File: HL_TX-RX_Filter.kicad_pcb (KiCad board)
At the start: 2 copper layers, 100 x 100 mm, 199 parts, among them J1 CNR1, J10 To Rx in, J2 CNR3, J3 CNR2, J4 CNR4, J5 To Antenna, J6 From Tx, J7 ICSP, J8 SCL SDA, J9 Input1, Q1 2N7002, Q2 2N7002, Q3 2N7002, Q4 2N7002, Q5 2N7002, Q6 2N7002, Q7 2N7002, Q8 2N7002, U1 ATMEGA328-AU, U10 PE4259, U11 PE4259, U12 PE4259, U2 PE4259, U3 PE4259, U4 PE4259, U5 PE4259, U6 PE4259, U7 PE4259, U8 PE4259, U9 PE4259

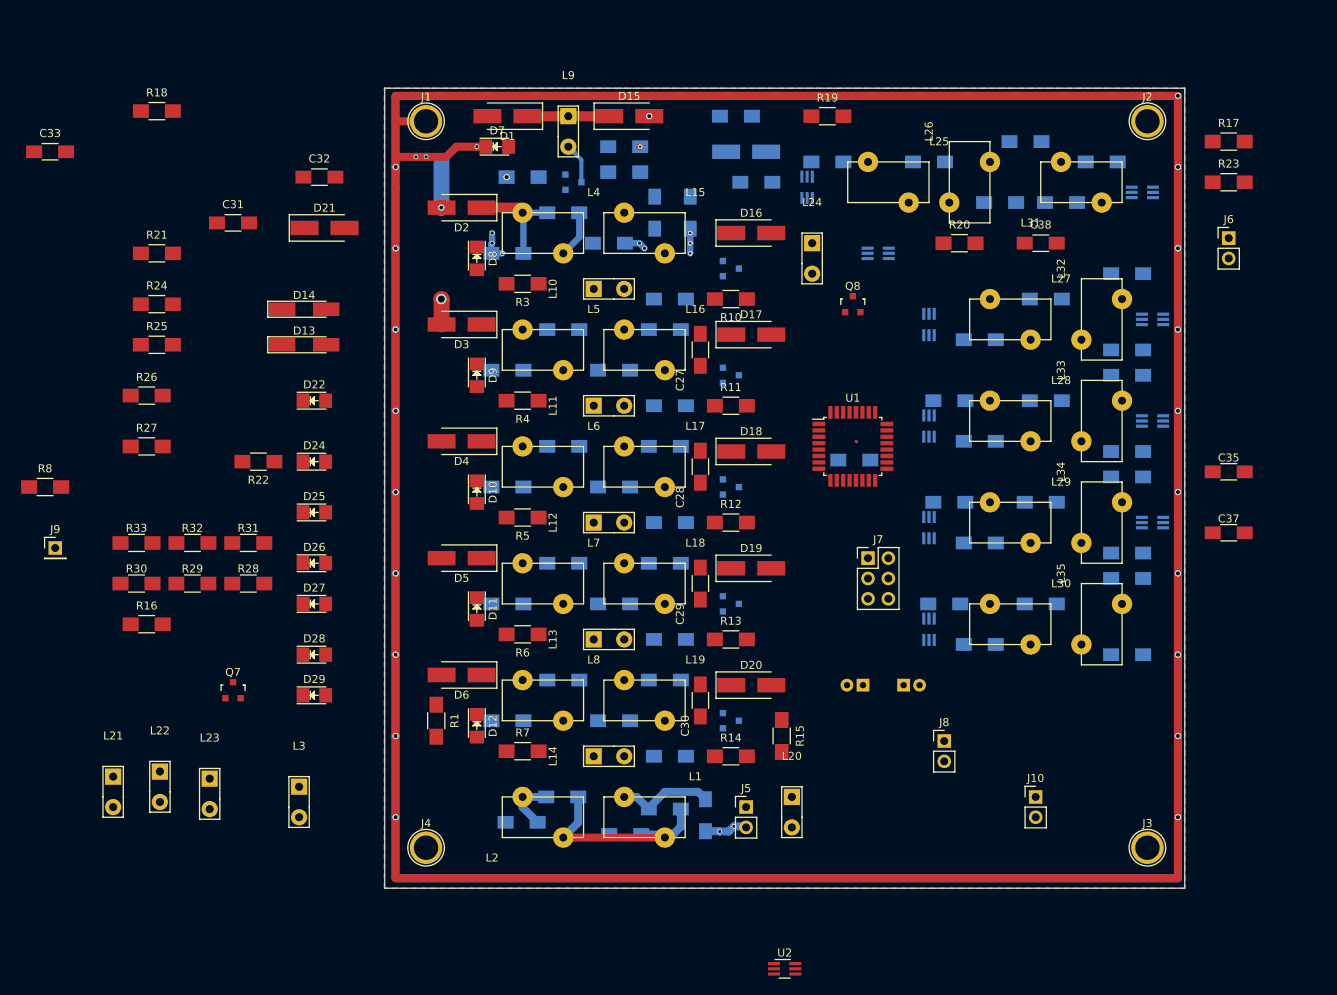
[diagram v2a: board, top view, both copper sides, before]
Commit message: Re-building PCB after annotation redo
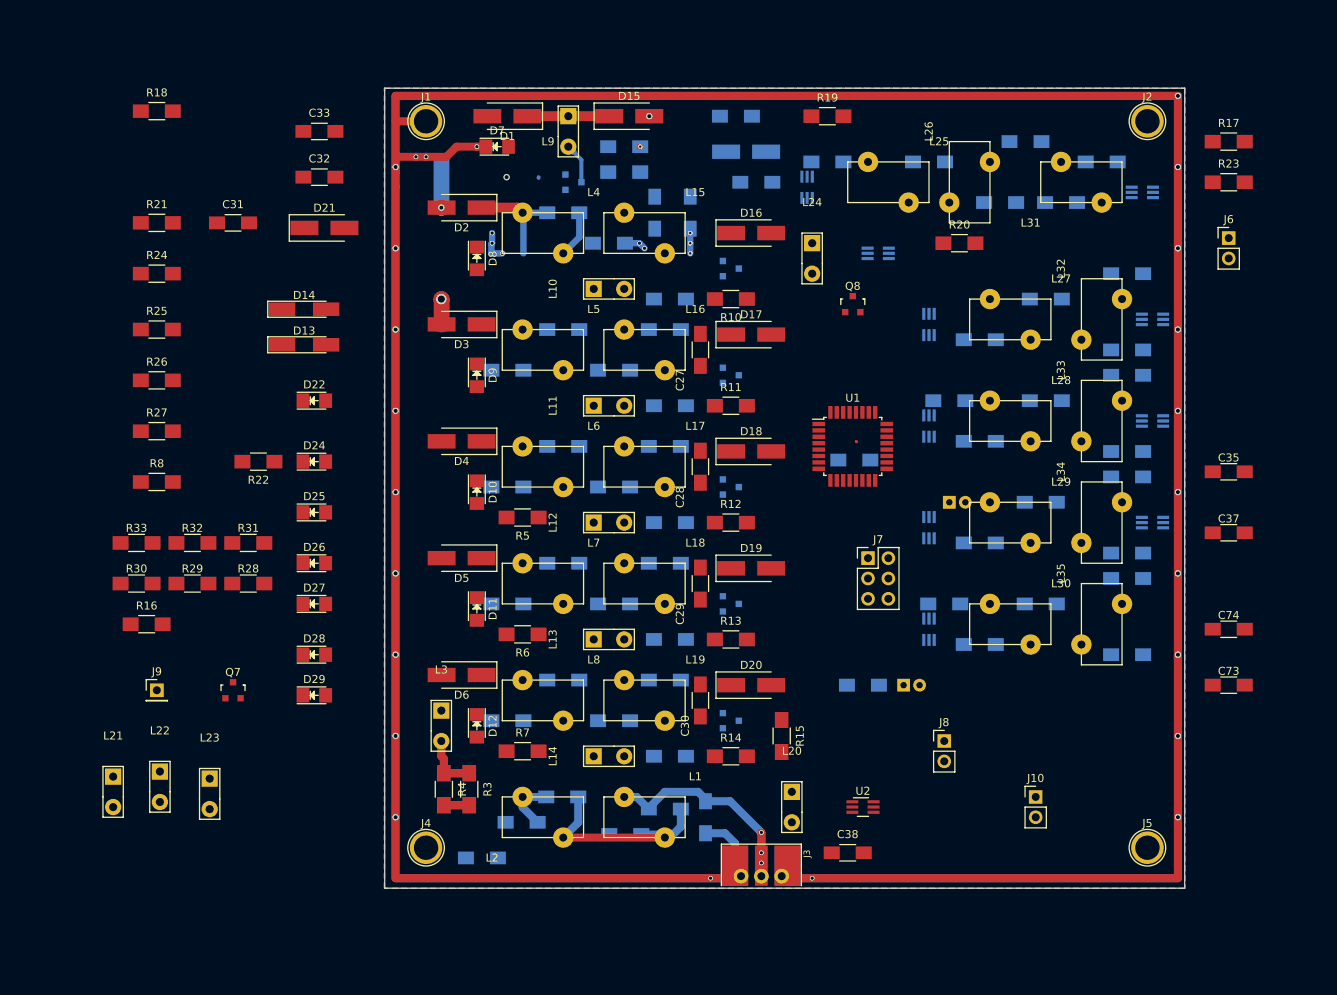
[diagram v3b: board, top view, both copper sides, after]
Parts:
- added C73: 680p, Capacitors_SMD:C_1206_HandSoldering, F.Cu at (230.5, 134.6)
- added C74: 360p, Capacitors_SMD:C_1206_HandSoldering, F.Cu at (230.5, 127.6)
- C10: value 1000p -> 540p
- C11: value 15p -> 1000p
- C12: value 39p -> 15p
- C13: value 68p -> 39p
- C14: value 82p -> 68p
- C15: value 180p -> 82p
- C16: value .1u -> 180p
- C22: value 300p -> .1u
- C23: value 560p -> 300p
- C24: value 1082p -> 560p
- C25: value 2100p -> 1082p
- C26: value 200p -> 2100p
- C27: value 43p -> 200p
- C28: value 130p -> 43p
- C29: value 220p -> 130p
- C30: value 270p -> 220p
- C31: value 552p -> 270p
- C32: value 74p -> 552p
- C33: value 120p -> 74p
- C34: value 180p -> 120p
- C35: value 390p -> 180p
- C36: value 736p -> 390p
- C37: value 22p -> 736p
- C38: value C -> .1u
- C39: value 0.1u -> 22p
- C40: value 0.1 -> C
- C41: value 4.7u -> 0.1u; footprint Capacitors_THT:CP_Radial_D5.0mm_P2.00mm -> Capacitors_SMD:C_1206_HandSoldering
- C42: value C -> 0.1
- C44: value 0.1u -> C
- C45: value 0.1u -> 4.7u; footprint Capacitors_SMD:C_1206_HandSoldering -> Capacitors_THT:CP_Radial_D5.0mm_P2.00mm
- C46: value 3000p -> 0.1u
- C47: value 0.012u -> 0.1u
- C48: value 1600p -> 3000p
- C49: value 1500p -> 0.012u
- C50: value 680p -> 1600p
- C51: value 470p -> 1500p
- C52: value 270p -> 680p
- C53: value 2400p -> 470p
- C54: value 8200p -> 270p
- C55: value 3900p -> 2400p
- C56: value 2400p -> 8200p
- C57: value 1500p -> 3900p
- C58: value 1800p -> 2400p
- C59: value 680p -> 1500p
- C6: value 100p -> .1u
- C60: value 340p -> 1800p
- C61: value 236p -> 680p
- C62: value 130p -> 340p
- C63: value 3000p -> 236p
- C64: value 2700p -> 130p
- C65: value 1220p -> 3000p
- C66: value 780p -> 2700p
- C67: value 510p -> 1220p
- C68: value 2400p -> 780p
- C69: value 2000p -> 510p
- C7: value 150p -> 100p
- C70: value 1000p -> 2400p
- C71: value 680p -> 2000p
- C72: value 360p -> 1000p
- C8: value 280p -> 150p
- C9: value 540p -> 280p
- J3: value CNR2 -> Antenna; footprint Connectors:1pin -> Connectors_G:SMAEDGE_TH
- J4: value CNR4 -> CNR2
- J5: value To Antenna -> CNR4; footprint Pin_Headers:Pin_Header_Straight_1x02_Pitch2.54mm -> Connectors:1pin
- R1: moved to B.Cu
- moved C38 79.9 mm to (182.9, 155.6)
- moved R2 77.1 mm to (132.4, 147.6), turned to 270 degrees
- moved C6 75.6 mm to (137.2, 156.2)
- moved R3 63.5 mm to (135.6, 147.6), turned to 270 degrees
- moved J5 50.4 mm to (220.3, 154.9)
- moved R4 49.6 mm to (132.4, 147.6), turned to 270 degrees
- moved J3 48.5 mm to (172.1, 159.9)
- moved C33 33.8 mm to (116.8, 65.4)
- moved U2 22.5 mm to (184.8, 149.9)
- moved J9 21.8 mm to (96.5, 135.3)
- moved L3 20.2 mm to (132.1, 137.8)
- moved R8 14.0 mm to (96.5, 109.2)
- moved R1 9.51 mm to (135.6, 147.6)
- moved R21 3.81 mm to (96.5, 76.8)
- moved R24 3.81 mm to (96.5, 83.2)
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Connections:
- C11 pad 2: Net-(C11-Pad2) -> GND
- C16 pad 1: Net-(C16-Pad1) -> Net-(C11-Pad1)
- C16 pad 2: GND -> Net-(C16-Pad2)
- C22 pad 1: Net-(C12-Pad2) -> Net-(C22-Pad1)
- C26 pad 1: Net-(C11-Pad2) -> Net-(C16-Pad2)
- C27 pad 1: Net-(C11-Pad2) -> Net-(C12-Pad2)
- C27 pad 2: Net-(C27-Pad2) -> GND
- C32 pad 1: Net-(C27-Pad2) -> Net-(C16-Pad2)
- C32 pad 2: GND -> Net-(C32-Pad2)
- C37 pad 1: Net-(C37-Pad1) -> Net-(C32-Pad2)
- C37 pad 2: Net-(C37-Pad2) -> GND
- C38 pad 1: Net-(C38-Pad1) -> GND
- C39 pad 1: Net-(C37-Pad2) -> Net-(C39-Pad1)
- C40 pad 1: 3V3 -> Net-(C40-Pad1)
- C40 pad 2: GND -> Net-(C40-Pad2)
- C41 pad 1: 3V3 -> Net-(C39-Pad2)
- C41 pad 2: GND -> Net-(C41-Pad2)
- C42 pad 1: Net-(C38-Pad1) -> 3V3
- C42 pad 2: Net-(C42-Pad2) -> GND
- C44 pad 1: Net-(C44-Pad1) -> Net-(C40-Pad1)
- C44 pad 2: GND -> Net-(C44-Pad2)
- C45 pad 1: Net-(C45-Pad1) -> 3V3
- C45 pad 2: Net-(C45-Pad2) -> GND
- C46 pad 2: Net-(C46-Pad2) -> GND
- C47 pad 2: GND -> Net-(C47-Pad2)
- C48 pad 1: Net-(C46-Pad2) -> Net-(C48-Pad1)
- C49 pad 2: Net-(C49-Pad2) -> GND
- C50 pad 1: Net-(C50-Pad1) -> Net-(C48-Pad2)
- C53 pad 2: GND -> Net-(C53-Pad2)
- C54 pad 2: GND -> Net-(C54-Pad2)
- C58 pad 1: Net-(C48-Pad2) -> Net-(C58-Pad1)
- C58 pad 2: Net-(C58-Pad2) -> GND
- C59 pad 1: Net-(C49-Pad2) -> Net-(C59-Pad1)
- C59 pad 2: Net-(C59-Pad2) -> GND
- C6 pad 1: Net-(C11-Pad1) -> GND
- C6 pad 2: GND -> Net-(C38-Pad2)
- C63 pad 1: Net-(C63-Pad1) -> Net-(C53-Pad2)
- C63 pad 2: GND -> Net-(C63-Pad2)
- C64 pad 1: Net-(C64-Pad1) -> Net-(C54-Pad2)
- C64 pad 2: GND -> Net-(C64-Pad2)
- C68 pad 1: Net-(C58-Pad2) -> Net-(C68-Pad1)
- C68 pad 2: Net-(C68-Pad2) -> GND
- C69 pad 1: Net-(C59-Pad2) -> Net-(C69-Pad1)
- C69 pad 2: Net-(C69-Pad2) -> GND
- D13 pad 1: Net-(C37-Pad1) -> Net-(C39-Pad1)
- D14 pad 1: Net-(C44-Pad1) -> Net-(C46-Pad1)
- D14 pad 2: Net-(C37-Pad1) -> Net-(C39-Pad1)
- D15 pad 2: Net-(C38-Pad1) -> Net-(C40-Pad1)
- D16 pad 1: Net-(C27-Pad2) -> Net-(C28-Pad2)
- D16 pad 2: Net-(C38-Pad1) -> Net-(C40-Pad1)
- D17 pad 1: Net-(C28-Pad2) -> Net-(C29-Pad2)
- D17 pad 2: Net-(C38-Pad1) -> Net-(C40-Pad1)
- D18 pad 1: Net-(C29-Pad2) -> Net-(C30-Pad2)
- D18 pad 2: Net-(C38-Pad1) -> Net-(C40-Pad1)
- D19 pad 1: Net-(C30-Pad2) -> Net-(C31-Pad2)
- D19 pad 2: Net-(C38-Pad1) -> Net-(C40-Pad1)
- D2 pad 1: Net-(C11-Pad1) -> Net-(C12-Pad1)
- D20 pad 1: Net-(C31-Pad2) -> Net-(C32-Pad2)
- D20 pad 2: Net-(C38-Pad1) -> Net-(C40-Pad1)
- D21 pad 1: Net-(C37-Pad2) -> Net-(C39-Pad2)
- D21 pad 2: Net-(C38-Pad2) -> Net-(C40-Pad2)
- D23 pad 1: Net-(C45-Pad1) -> Net-(C47-Pad1)
- D23 pad 2: Net-(C42-Pad2) -> Net-(C44-Pad2)
- D3 pad 1: Net-(C12-Pad1) -> Net-(C13-Pad1)
- D4 pad 1: Net-(C13-Pad1) -> Net-(C14-Pad1)
- D5 pad 1: Net-(C14-Pad1) -> Net-(C10-Pad1)
- D6 pad 1: Net-(C10-Pad1) -> Net-(C11-Pad1)
- J3 pad 1: GND -> Net-(C1-Pad2)
- J5 pad 1: Net-(C1-Pad2) -> GND
- J6 pad 1: Net-(C39-Pad2) -> Net-(C41-Pad2)
- L10 pad 1: Net-(C11-Pad2) -> Net-(C12-Pad2)
- L10 pad 2: Net-(C17-Pad1) -> Net-(C18-Pad1)
- L11 pad 1: Net-(C12-Pad2) -> Net-(C13-Pad2)
- L11 pad 2: Net-(C18-Pad1) -> Net-(C19-Pad1)
- L12 pad 1: Net-(C13-Pad2) -> Net-(C14-Pad2)
- L12 pad 2: Net-(C19-Pad1) -> Net-(C20-Pad1)
- L13 pad 1: Net-(C14-Pad2) -> Net-(C15-Pad2)
- L13 pad 2: Net-(C20-Pad1) -> Net-(C21-Pad1)
- L14 pad 1: Net-(C15-Pad2) -> Net-(C16-Pad2)
- L14 pad 2: Net-(C21-Pad1) -> Net-(C22-Pad1)
- L15 pad 1: Net-(C11-Pad2) -> Net-(C12-Pad2)
- L15 pad 2: Net-(C27-Pad2) -> Net-(C28-Pad2)
- L16 pad 1: Net-(C12-Pad2) -> Net-(C13-Pad2)
- L16 pad 2: Net-(C28-Pad2) -> Net-(C29-Pad2)
- L17 pad 1: Net-(C13-Pad2) -> Net-(C14-Pad2)
- L17 pad 2: Net-(C29-Pad2) -> Net-(C30-Pad2)
- L18 pad 1: Net-(C14-Pad2) -> Net-(C15-Pad2)
- L18 pad 2: Net-(C30-Pad2) -> Net-(C31-Pad2)
- L19 pad 1: Net-(C15-Pad2) -> Net-(C16-Pad2)
- L19 pad 2: Net-(C31-Pad2) -> Net-(C32-Pad2)
- L20 pad 1: Net-(L20-Pad1) -> Net-(C40-Pad1)
- L22 pad 1: Net-(C37-Pad2) -> Net-(C39-Pad2)
- L24 pad 1: Net-(C45-Pad1) -> Net-(C47-Pad1)
- L25 pad 1: Net-(C47-Pad1) -> Net-(C49-Pad1)
- L25 pad 2: Net-(C46-Pad2) -> Net-(C48-Pad2)
- L26 pad 1: Net-(C48-Pad2) -> Net-(C50-Pad2)
- L26 pad 2: Net-(C53-Pad1) -> Net-(C55-Pad1)
- L27 pad 1: Net-(C54-Pad1) -> Net-(C56-Pad1)
- L27 pad 2: Net-(C49-Pad2) -> Net-(C51-Pad2)
- L28 pad 1: Net-(C55-Pad1) -> Net-(C57-Pad1)
- L28 pad 2: Net-(C50-Pad2) -> Net-(C52-Pad2)
- L29 pad 1: Net-(C56-Pad1) -> Net-(C58-Pad1)
- L29 pad 2: Net-(C51-Pad2) -> Net-(C53-Pad2)
- L3 pad 1: Net-(L3-Pad1) -> Net-(C2-Pad1)
- L3 pad 2: Net-(L20-Pad2) -> Net-(L3-Pad2)
- L30 pad 1: Net-(C57-Pad1) -> Net-(C59-Pad1)
- L30 pad 2: Net-(C52-Pad2) -> Net-(C54-Pad2)
- L31 pad 1: Net-(C58-Pad2) -> Net-(C60-Pad2)
- L31 pad 2: Net-(C63-Pad1) -> Net-(C65-Pad1)
- L32 pad 1: Net-(C59-Pad2) -> Net-(C61-Pad2)
- L32 pad 2: Net-(C64-Pad1) -> Net-(C66-Pad1)
- L33 pad 1: Net-(C60-Pad2) -> Net-(C62-Pad2)
- L33 pad 2: Net-(C65-Pad1) -> Net-(C67-Pad1)
- L34 pad 1: Net-(C61-Pad2) -> Net-(C63-Pad2)
- L34 pad 2: Net-(C66-Pad1) -> Net-(C68-Pad1)
- L35 pad 1: Net-(C62-Pad2) -> Net-(C64-Pad2)
- L35 pad 2: Net-(C67-Pad1) -> Net-(C69-Pad1)
- L4 pad 1: Net-(C11-Pad2) -> Net-(C12-Pad2)
- L4 pad 2: Net-(C11-Pad1) -> Net-(C12-Pad1)
- L5 pad 1: Net-(C12-Pad2) -> Net-(C13-Pad2)
- L5 pad 2: Net-(C12-Pad1) -> Net-(C13-Pad1)
- L6 pad 1: Net-(C13-Pad2) -> Net-(C14-Pad2)
- L6 pad 2: Net-(C13-Pad1) -> Net-(C14-Pad1)
- L7 pad 1: Net-(C14-Pad2) -> Net-(C15-Pad2)
- L7 pad 2: Net-(C14-Pad1) -> Net-(C10-Pad1)
- L8 pad 1: Net-(C15-Pad2) -> Net-(C16-Pad2)
- L8 pad 2: Net-(C10-Pad1) -> Net-(C11-Pad1)
- L9 pad 2: Net-(C16-Pad1) -> Net-(C17-Pad1)
- Q1 pad 3: Net-(C16-Pad1) -> Net-(C17-Pad1)
- Q2 pad 3: Net-(C17-Pad1) -> Net-(C18-Pad1)
- Q3 pad 3: Net-(C18-Pad1) -> Net-(C19-Pad1)
- Q4 pad 3: Net-(C19-Pad1) -> Net-(C20-Pad1)
- Q5 pad 3: Net-(C20-Pad1) -> Net-(C21-Pad1)
- Q6 pad 3: Net-(C21-Pad1) -> Net-(C22-Pad1)
- R1 pad 1: Net-(C2-Pad1) -> Net-(L3-Pad2)
- R1 pad 2: Net-(L3-Pad1) -> Net-(C38-Pad2)
- R11 pad 2: (no net) -> +12V
- R12 pad 1: Net-(C44-Pad1) -> Net-(C46-Pad1)
- R12 pad 2: Net-(C16-Pad1) -> Net-(C17-Pad1)
- R13 pad 1: Net-(C44-Pad1) -> Net-(C46-Pad1)
- R13 pad 2: Net-(C17-Pad1) -> Net-(C18-Pad1)
- R14 pad 1: Net-(C44-Pad1) -> Net-(C46-Pad1)
- R14 pad 2: Net-(C18-Pad1) -> Net-(C19-Pad1)
- R15 pad 1: Net-(C44-Pad1) -> Net-(C46-Pad1)
- R15 pad 2: Net-(C19-Pad1) -> Net-(C20-Pad1)
- R16 pad 1: Net-(C44-Pad1) -> Net-(C46-Pad1)
- R16 pad 2: Net-(C20-Pad1) -> Net-(C21-Pad1)
- R17 pad 1: Net-(C44-Pad1) -> Net-(C46-Pad1)
- R17 pad 2: Net-(C21-Pad1) -> Net-(C22-Pad1)
- R18 pad 1: Net-(C38-Pad1) -> Net-(L20-Pad2)
- R18 pad 2: Net-(L20-Pad1) -> Net-(C38-Pad2)
- R19 pad 1: Net-(C38-Pad1) -> Net-(L20-Pad2)
- R19 pad 2: Net-(L20-Pad1) -> Net-(C38-Pad2)
- R2 pad 1: Net-(C2-Pad1) -> Net-(L3-Pad2)
- R2 pad 2: Net-(L3-Pad1) -> Net-(C38-Pad2)
- R20 pad 1: Net-(C38-Pad1) -> Net-(L20-Pad2)
- R20 pad 2: Net-(L20-Pad1) -> Net-(C38-Pad2)
- R21 pad 1: Net-(C38-Pad1) -> Net-(L20-Pad2)
- R21 pad 2: Net-(L20-Pad1) -> Net-(C38-Pad2)
- R22 pad 1: Net-(C38-Pad2) -> Net-(C40-Pad2)
- R23 pad 2: Net-(C44-Pad1) -> Net-(C46-Pad1)
- R25 pad 2: Net-(C42-Pad2) -> Net-(C44-Pad2)
- R26 pad 2: Net-(C44-Pad1) -> Net-(C46-Pad1)
- R3 pad 1: Net-(C2-Pad1) -> Net-(L3-Pad2)
- R3 pad 2: Net-(L3-Pad1) -> Net-(C38-Pad2)
- R4 pad 1: Net-(C2-Pad1) -> Net-(L3-Pad2)
- R4 pad 2: Net-(L3-Pad1) -> Net-(C38-Pad2)
- U1 pad 19: (no net) -> Net-(U1-Pad19)
- U1 pad 20: (no net) -> Net-(U1-Pad20)
- U1 pad 22: (no net) -> Net-(U1-Pad22)
- U1 pad 30: (no net) -> Net-(U1-Pad30)
- U1 pad 31: (no net) -> Net-(U1-Pad31)
- U10 pad 1: Net-(C70-Pad2) -> Net-(C72-Pad2)
- U10 pad 3: (no net) -> Net-(U10-Pad3)
- U11 pad 1: Net-(C71-Pad2) -> Net-(C73-Pad2)
- U11 pad 3: (no net) -> Net-(U11-Pad3)
- U12 pad 1: Net-(C72-Pad2) -> Net-(C74-Pad2)
- U12 pad 3: (no net) -> Net-(U12-Pad3)
- U2 pad 1: Net-(C46-Pad1) -> Net-(C48-Pad1)
- U2 pad 5: Net-(C45-Pad2) -> Net-(C47-Pad2)
- U3 pad 3: (no net) -> Net-(U3-Pad3)
- U4 pad 1: Net-(C49-Pad1) -> Net-(C51-Pad1)
- U4 pad 3: (no net) -> Net-(U4-Pad3)
- U5 pad 1: Net-(C50-Pad1) -> Net-(C52-Pad1)
- U5 pad 3: (no net) -> Net-(U5-Pad3)
- U6 pad 1: Net-(C51-Pad1) -> Net-(C53-Pad1)
- U6 pad 3: (no net) -> Net-(U6-Pad3)
- U7 pad 1: Net-(C52-Pad1) -> Net-(C54-Pad1)
- U7 pad 3: (no net) -> Net-(U7-Pad3)
- U8 pad 1: Net-(C68-Pad2) -> Net-(C70-Pad2)
- U8 pad 3: (no net) -> Net-(U8-Pad3)
- U9 pad 1: Net-(C69-Pad2) -> Net-(C71-Pad2)
- U9 pad 3: (no net) -> Net-(U9-Pad3)
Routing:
- net Net-(C1-Pad2): track 12.4 -> 32.1 mm, vias 0 -> 3
- net Net-(L3-Pad2): track 0.00 -> 14.7 mm
- net Net-(C12-Pad1): track 0.00 -> 13.6 mm
- net Net-(C11-Pad1): track 13.6 -> 0.13 mm
- net GND: track 813.9 -> 801.6 mm, vias 33 -> 28
- net Net-(C38-Pad2): track 0.00 -> 6.35 mm
- net Net-(C16-Pad1): track 6.15 -> 0.00 mm
- net Net-(C17-Pad1): track 0.00 -> 6.02 mm
- net Net-(C11-Pad2): track 5.91 -> 0.00 mm
- net (no net): track 0.06 -> 4.10 mm, vias 0 -> 4
- net Net-(C12-Pad2): track 0.00 -> 2.83 mm
- net Net-(C16-Pad2): track 0.00 -> 2.71 mm, vias 0 -> 2
- net Net-(C40-Pad1): track 0.00 -> 0.58 mm, vias 0 -> 1
- net 3V3: track 0.58 -> 0.00 mm
- net Net-(L3-Pad1): vias 1 -> 0
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
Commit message: Rearranging layout for re-annotated schematic
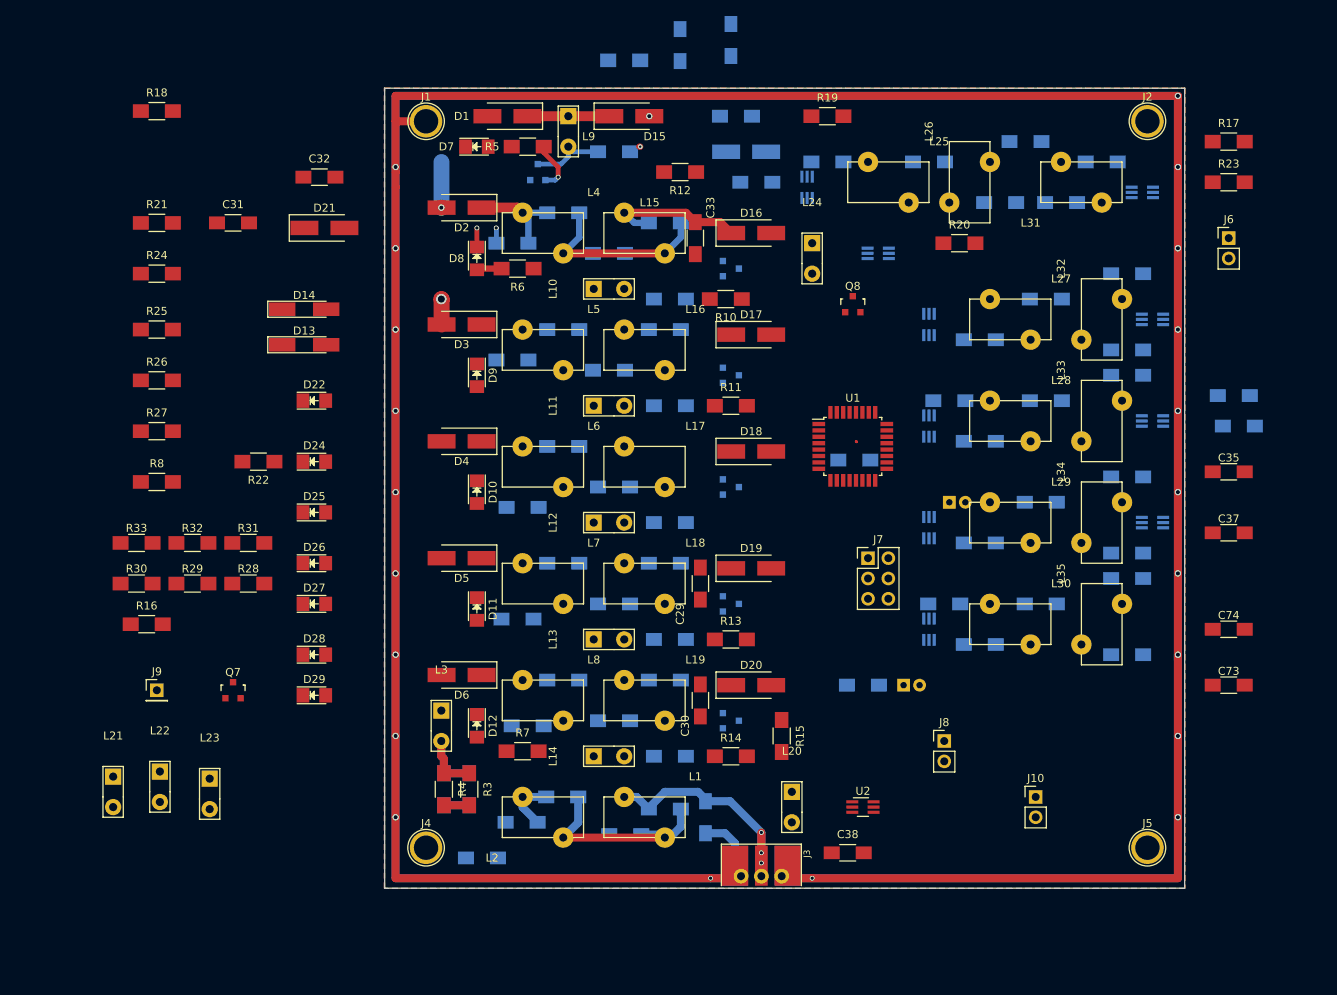
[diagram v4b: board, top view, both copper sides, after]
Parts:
- C27, C28: moved to B.Cu
- moved C67 84.4 mm to (231.8, 102.2)
- moved C11 64.3 mm to (142.9, 139.7)
- moved C16 54.9 mm to (147.3, 134.0)
- moved C33 48.8 mm to (163.8, 78.7), turned to 270 degrees
- moved R5 46.4 mm to (142.9, 67.3)
- moved R6 45.7 mm to (141.6, 82.5)
- moved R12 44.3 mm to (161.9, 70.5), turned to 180 degrees
- moved C28 30.8 mm to (160.0, 76.8), turned to 180 degrees
- moved C17 27.3 mm to (153.7, 67.9)
- moved C26 22.2 mm to (168.3, 54.0)
- moved C21 21.2 mm to (161.9, 54.6)
- moved C27 16.6 mm to (153.0, 80.6), turned to 0 degrees
- moved C7 15.9 mm to (141.0, 79.4)
- moved C8 15.9 mm to (141.0, 94.0)
- moved C59 15.1 mm to (231.1, 98.4)
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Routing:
- net Net-(C12-Pad2): track 2.83 -> 27.0 mm
- net Net-(C28-Pad2): track 0.00 -> 18.0 mm
- net GND: track 801.6 -> 787.3 mm, vias 28 -> 23
- net /T0: track 0.00 -> 6.30 mm, vias 0 -> 1
- net (no net): track 4.10 -> 0.15 mm, vias 4 -> 1
- net Net-(C17-Pad1): track 6.02 -> 9.43 mm
- net Net-(D8-Pad2): track 0.00 -> 3.14 mm
- net Net-(C16-Pad2): track 2.71 -> 0.00 mm, vias 2 -> 0
- net Net-(C12-Pad1): track 13.6 -> 12.7 mm

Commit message: More layout progress
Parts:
- C29, C30, C31, C32, R12, R13, R14, R15, R16, R17: moved to B.Cu
- C34, C36, R9: moved to F.Cu
- moved R17 99.9 mm to (168.3, 144.8), turned to 180 degrees
- moved C26 86.3 mm to (153.7, 139.1), turned to 0 degrees
- moved C71 80.8 mm to (230.5, 88.3)
- moved C32 77.3 mm to (160.0, 135.3), turned to 180 degrees
- moved C21 75.6 mm to (160.7, 130.2), turned to 0 degrees
- moved C68 75.6 mm to (229.2, 118.1)
- moved R16 73.1 mm to (168.3, 130.2), turned to 180 degrees
- moved R9 71.1 mm to (141.6, 126.4)
- moved C37 70.1 mm to (163.8, 137.2), turned to 270 degrees
- moved C31 69.5 mm to (160.0, 120.7), turned to 180 degrees
- moved C35 66.7 mm to (163.8, 108.0), turned to 270 degrees
- moved R10 60.5 mm to (141.6, 141.0)
- moved C36 59.3 mm to (163.8, 122.6), turned to 270 degrees
- moved R11 59.1 mm to (109.2, 99.1)
- moved C69 57.1 mm to (106.0, 83.2)
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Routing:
- net Net-(C46-Pad1): track 0.00 -> 93.7 mm
- net Net-(C2-Pad1): track 16.0 -> 85.9 mm, vias 2 -> 10
- net Net-(C40-Pad1): track 0.58 -> 63.5 mm, vias 1 -> 9
- net /T160: track 0.00 -> 36.4 mm, vias 0 -> 3
- net /T80: track 0.00 -> 35.7 mm, vias 0 -> 3
- net Net-(C15-Pad2): track 0.00 -> 32.0 mm
- net Net-(C14-Pad2): track 0.00 -> 32.0 mm
- net Net-(C16-Pad2): track 0.00 -> 32.0 mm
- net Net-(C13-Pad2): track 0.00 -> 31.4 mm
- net /T17: track 0.00 -> 25.8 mm, vias 0 -> 1
- net /T30: track 0.00 -> 25.2 mm, vias 0 -> 1
- net /T40: track 0.00 -> 25.2 mm, vias 0 -> 1
- net Net-(C31-Pad2): track 0.00 -> 17.5 mm
- net Net-(C30-Pad2): track 0.00 -> 17.5 mm
- net Net-(C32-Pad2): track 0.00 -> 17.5 mm
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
